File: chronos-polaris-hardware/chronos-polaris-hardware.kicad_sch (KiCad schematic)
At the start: 58 parts, among them J1 Conn_01x03_Pin, J2 Conn_01x03_Pin, J3 Conn_01x03_Pin, J4 Conn_01x03_Pin, J5 Conn_01x03_Pin, J6 Conn_01x04, J7 Conn_01x04, J8 Conn_01x02, P1 WJ124-3_81-6P, U1 TPS62172DSGR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

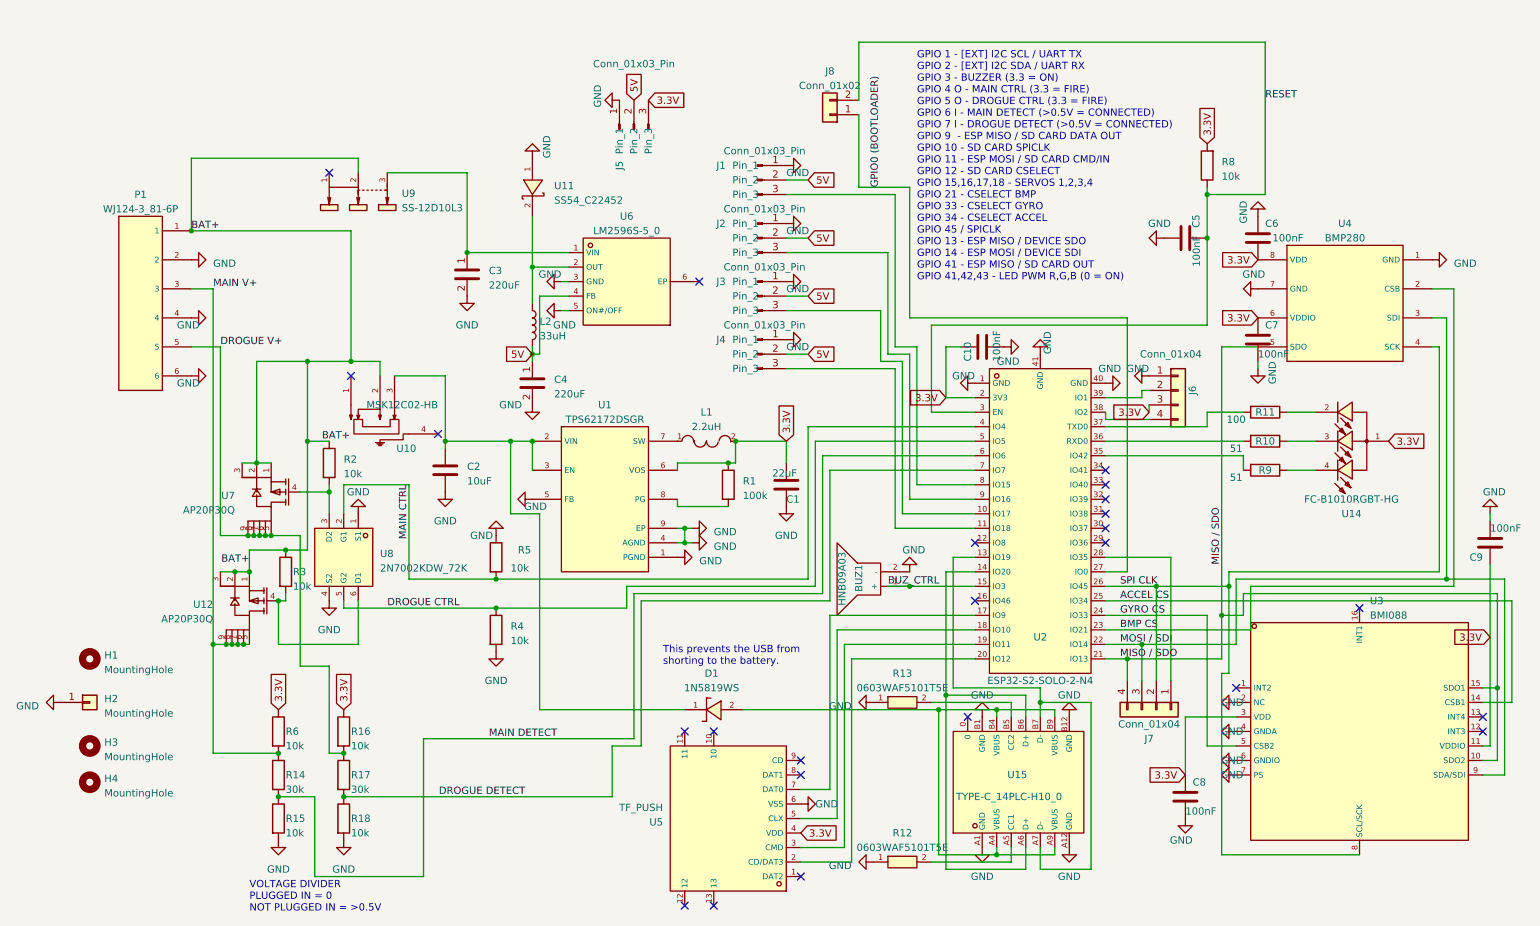
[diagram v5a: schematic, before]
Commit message: switch to compact 5v regulator
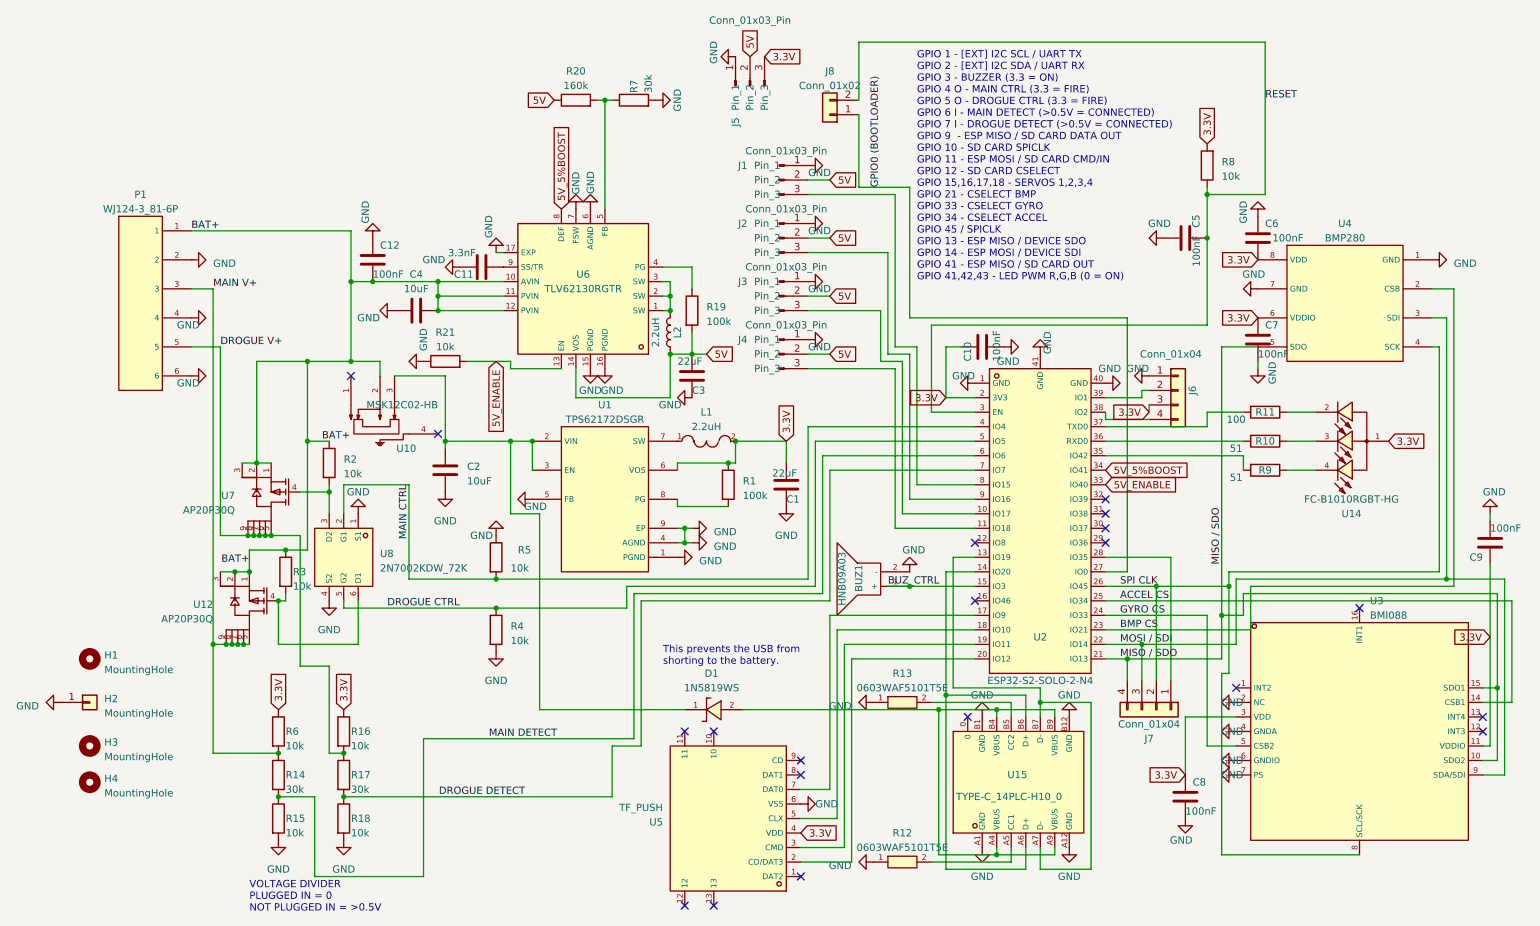
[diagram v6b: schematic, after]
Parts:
- removed U11: SS54_C22452, polaris-fp:SMA_L4.4-W2.8-LS5.4-R-RD, symbol polaris-sym:SS54_C22452
- removed U6: LM2596S-5_0, polaris-fp:TO-263-5_L10.2-W8.9-P1.70-BR, symbol polaris-sym:LM2596S-5_0
- removed U9: SS-12D10L3, polaris-fp:SW-TH_SS-12D10L3, symbol polaris-sym:SS-12D10L3
- added C11: 3.3nF, Capacitor_SMD:C_0402_1005Metric, symbol Device:C
- added C12: 100nF, Capacitor_SMD:C_0402_1005Metric, symbol Device:C
- added R19: 100k, Resistor_SMD:R_0603_1608Metric, symbol Device:R
- added R20: 160k, Resistor_SMD:R_0603_1608Metric, symbol Device:R
- added R21: 10k, Resistor_SMD:R_0603_1608Metric, symbol Device:R
- added R7: 30k, Resistor_SMD:R_0603_1608Metric, symbol Device:R
- added U6: TLV62130RGTR, polaris-fp:QFN-16_L3.0-W3.0-P0.50-TL-EP, symbol polaris-sym:TLV62130RGTR
- C3: value 220uF -> 22uF; footprint Capacitor_SMD:CP_Elec_8x10.5 -> Capacitor_SMD:C_0603_1608Metric
- C4: value 220uF -> 10uF; footprint Capacitor_SMD:CP_Elec_8x10.5 -> Capacitor_SMD:C_0805_2012Metric
- L2: value 33uH -> 2.2uH; footprint polaris-fp:IND-SMD_L11.5-W10.0_SMMS1040 -> polaris-fp:IND-SMD_L4.0-W4.0
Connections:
- net 5V: now also C3.1, L2.1, R19.2, R20.1, U6.14 (VOS); no longer C4.1, L2.2
- net BAT+: now also C4.1, C12.2, U6.10 (AVIN), U6.11 (PVIN), U6.12 (PVIN)
- net GND: now also C11.1, C12.1, R21.1, R7.2, U6.15 (PGND), U6.16 (PGND), U6.17 (EXP), U6.6 (AGND), U6.7 (FSW)
- net 5V_ENABLE: now reaches U2.33 (IO40)
- net 5V_ENABLE: now also R21.2, U6.13 (EN)
- net 5V_5%BOOST: now reaches U2.34 (IO41)
- net 5V_5%BOOST: now also U6.8 (DEF)
- new net: L2.2, U6.1 (SW), U6.2 (SW), U6.3 (SW)
- new net: R19.1, U6.4 (PG)
- new net: R20.2, R7.1, U6.5 (FB)
- new net: C11.2, U6.9 (SS/TR)
- no-connect marks 24 -> 20
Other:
- moved on the sheet: J1, J2, J3, J4, J5

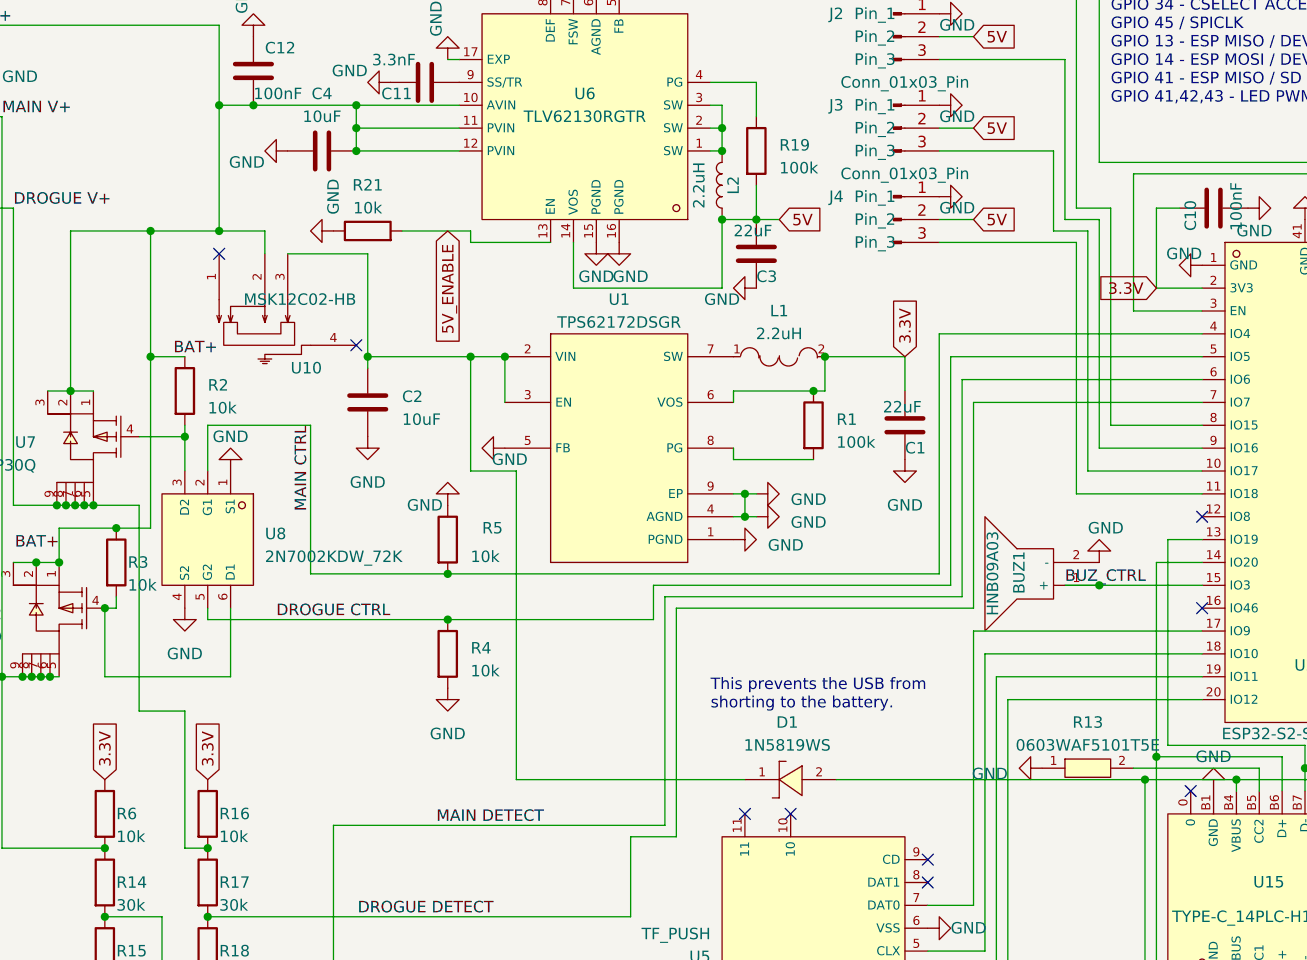
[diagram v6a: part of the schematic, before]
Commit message: fix V in switching with usb, remove diode
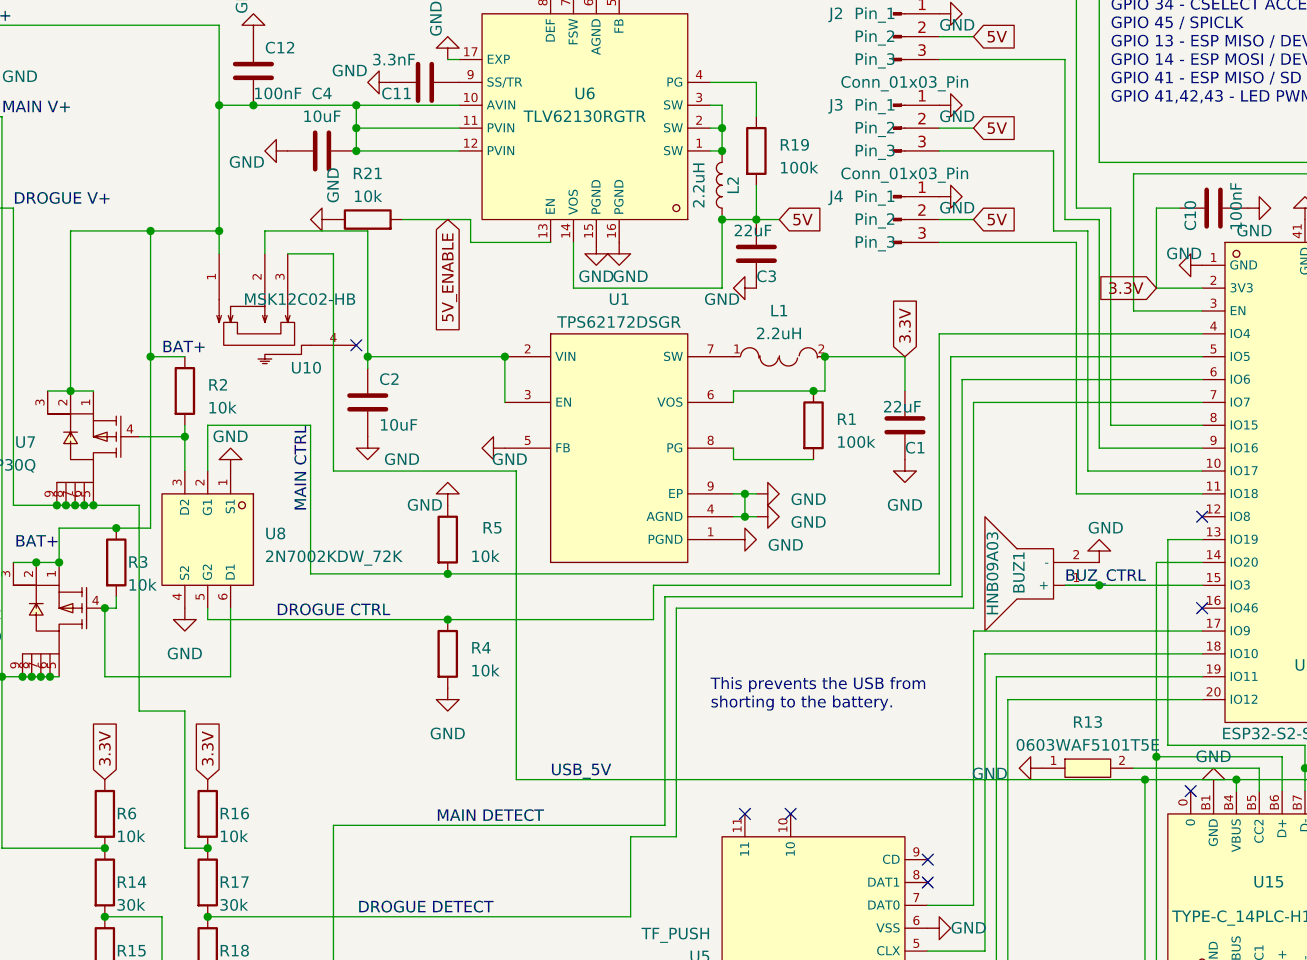
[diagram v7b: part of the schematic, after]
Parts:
- removed D1: 1N5819WS, polaris-fp:SOD-323_L1.8-W1.3-LS2.5-RD, symbol polaris-sym:1N5819WS
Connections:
- net BAT+: now also U10.1; no longer U10.2
- net at C2.1, U1.2 (VIN), U1.3 (EN): now also U10.2; no longer U10.3
- net USB_5V: now reaches U15.A4 (VBUS), U15.A9 (VBUS), U15.B4 (VBUS), U15.B9 (VBUS)
- net USB_5V: now also U10.3
- no-connect marks 20 -> 19
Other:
- moved on the sheet: R21
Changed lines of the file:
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@@
   (junction (at 194.31 137.16) (diameter 0) (color 0 0 0 0)
   )
-  (junction (at 109.22 90.17) (diameter 0) (color 0 0 0 0)
-  )
   (junction (at 80.01 144.78) (diameter 0) (color 0 0 0 0)
   )
@@
   (no_connect (at 160.02 148.59))
   (no_connect (at 257.81 119.38))
-  (no_connect (at 81.28 78.74))
   (wire (pts (xy 179.07 115.57) (xy 190.5 115.57))
     (stroke (width 0) (type default))
@@
     (stroke (width 0) (type default))
   )
-  (wire (pts (xy 86.36 76.2) (xy 86.36 78.74))
-    (stroke (width 0) (type default))
-  )
   (wire (pts (xy 166.37 156.21) (xy 166.37 123.19))
     (stroke (width 0) (type default))
@@
     (stroke (width 0) (type default))
   )
+  (wire (pts (xy 86.36 78.74) (xy 86.36 76.2))
+    (stroke (width 0) (type default))
+  )
   (wire (pts (xy 224.79 110.49) (xy 213.36 110.49))
     (stroke (width 0) (type default))
@@
     (stroke (width 0) (type default))
   )
-  (wire (pts (xy 73.66 90.17) (xy 77.47 90.17))
-    (stroke (width 0) (type default))
-  )
   (wire (pts (xy 139.7 105.41) (xy 139.7 107.95))
     (stroke (width 0) (type default))
@@
     (stroke (width 0) (type default))
   )
-  (wire (pts (xy 109.22 76.2) (xy 109.22 77.47))
+  (wire (pts (xy 109.22 74.93) (xy 109.22 77.47))
     (stroke (width 0) (type default))
   )
@@
     (stroke (width 0) (type default))
   )
+  (wire (pts (xy 73.66 90.17) (xy 77.47 90.17))
+    (stroke (width 0) (type default))
+  )
   (wire (pts (xy 233.68 73.66) (xy 233.68 120.65))
     (stroke (width 0) (type default))
@@
     (stroke (width 0) (type default))
   )
-  (wire (pts (xy 109.22 102.87) (xy 109.22 90.17))
-    (stroke (width 0) (type default))
-  )
   (wire (pts (xy 62.23 93.98) (xy 64.77 93.98))
     (stroke (width 0) (type default))
@@
     (stroke (width 0) (type default))
   )
-  (wire (pts (xy 109.22 90.17) (xy 113.03 90.17))
+  (wire (pts (xy 97.79 90.17) (xy 113.03 90.17))
     (stroke (width 0) (type default))
   )
@@
     (stroke (width 0) (type default))
   )
-  (wire (pts (xy 114.3 102.87) (xy 109.22 102.87))
-    (stroke (width 0) (type default))
-  )
   (wire (pts (xy 74.93 152.4) (xy 68.58 152.4))
     (stroke (width 0) (type default))
@@
     (stroke (width 0) (type default))
   )
+  (wire (pts (xy 93.98 78.74) (xy 88.9 78.74))
+    (stroke (width 0) (type default))
+  )
   (wire (pts (xy 60.96 113.03) (xy 63.5 113.03))
     (stroke (width 0) (type default))
@@
     (stroke (width 0) (type default))
   )
+  (wire (pts (xy 93.98 102.87) (xy 114.3 102.87))
+    (stroke (width 0) (type default))
+  )
+  (wire (pts (xy 81.28 76.2) (xy 81.28 78.74))
+    (stroke (width 0) (type default))
+  )
   (wire (pts (xy 130.81 116.84) (xy 163.83 116.84))
     (stroke (width 0) (type default))
@@
     (stroke (width 0) (type default))
   )
-  (wire (pts (xy 82.55 125.73) (xy 82.55 118.11))
+  (wire (pts (xy 86.36 76.2) (xy 97.79 76.2))
     (stroke (width 0) (type default))
   )
-  (wire (pts (xy 88.9 78.74) (xy 97.79 78.74))
+  (wire (pts (xy 82.55 125.73) (xy 82.55 118.11))
     (stroke (width 0) (type default))
   )
@@
     (stroke (width 0) (type default))
   )
+  (wire (pts (xy 93.98 102.87) (xy 93.98 78.74))
+    (stroke (width 0) (type default))
+  )
   (wire (pts (xy 160.02 163.83) (xy 168.91 163.83))
     (stroke (width 0) (type default))
@@
     (stroke (width 0) (type default))
   )
-  (wire (pts (xy 97.79 90.17) (xy 109.22 90.17))
-    (stroke (width 0) (type default))
-  )
   (wire (pts (xy 238.76 123.19) (xy 238.76 115.57))
     (stroke (width 0) (type default))
@@
     (stroke (width 0) (type default))
   )
-  (wire (pts (xy 139.7 137.16) (xy 114.3 137.16))
+  (wire (pts (xy 114.3 137.16) (xy 184.15 137.16))
     (stroke (width 0) (type default))
   )
@@
     (stroke (width 0) (type default))
   )
-  (wire (pts (xy 86.36 76.2) (xy 81.28 76.2))
-    (stroke (width 0) (type default))
-  )
   (wire (pts (xy 163.83 92.71) (xy 190.5 92.71))
     (stroke (width 0) (type default))
@@
     (stroke (width 0) (type default))
   )
-  (wire (pts (xy 97.79 78.74) (xy 97.79 90.17))
-    (stroke (width 0) (type default))
-  )
   (wire (pts (xy 165.1 54.61) (xy 161.29 54.61))
     (stroke (width 0) (type default))
@@
     (stroke (width 0) (type default))
   )
-  (wire (pts (xy 101.6 76.2) (xy 109.22 76.2))
-    (stroke (width 0) (type default))
-  )
-  (wire (pts (xy 149.86 137.16) (xy 184.15 137.16))
+  (wire (pts (xy 101.6 74.93) (xy 109.22 74.93))
     (stroke (width 0) (type default))
   )
@@
     (stroke (width 0) (type default))
   )
+  (wire (pts (xy 97.79 76.2) (xy 97.79 90.17))
+    (stroke (width 0) (type default))
+  )
   (wire (pts (xy 148.59 90.17) (xy 148.59 93.98))
     (stroke (width 0) (type default))
@@
     (effects (font (size 1.27 1.27)) (justify right bottom))
   )
+  (label "USB_5V" (at 118.11 137.16 0) (fields_autoplaced)
+    (effects (font (size 1.27 1.27)) (justify left bottom))
+  )
   (label "MAIN CTRL" (at 91.44 97.79 270) (fields_autoplaced)
     (effects (font (size 1.27 1.27)) (justify right bottom))
@@
     (effects (font (size 1.27 1.27)) (justify left bottom))
   )
-  (label "BAT+" (at 76.2 90.17 0) (fields_autoplaced)
+  (label "BAT+" (at 74.93 90.17 0) (fields_autoplaced)
     (effects (font (size 1.27 1.27)) (justify left bottom))
   )
@@
     (effects (font (size 1.27 1.27)) (justify left bottom))
   )
-  (global_label "5V_ENABLE" (shape input) (at 106.68 76.2 270) (fields_autoplaced)
+  (global_label "5V_ENABLE" (shape input) (at 106.68 74.93 270) (fields_autoplaced)
     (effects (font (size 1.27 1.27)) (justify right))
-    (property "Intersheetrefs" "${INTERSHEET_REFS}" (at 106.68 89.3867 90)
+    (property "Intersheetrefs" "${INTERSHEET_REFS}" (at 106.68 88.1167 90)
       (effects (font (size 1.27 1.27)) (justify right) hide)
     )
@@
     )
   )
-  (symbol (lib_id "polaris-sym:1N5819WS") (at 144.78 137.16 0) (unit 1)
-    (in_bom yes) (on_board yes) (dnp no) (fields_autoplaced)
-    (property "Reference" "D1" (at 144.399 130.81 0)
-      (effects (font (size 1.27 1.27)))
-    )
-    (property "Value" "1N5819WS" (at 144.399 133.35 0)
-      (effects (font (size 1.27 1.27)))
-    )
-    (property "Footprint" "polaris-fp:SOD-323_L1.8-W1.3-LS2.5-RD" (at 144.78 147.32 0)
-      (effects (font (size 1.27 1.27) italic) hide)
-    )
-    (property "Datasheet" "https://item.szlcsc.com/295156.html" (at 142.494 137.033 0)
-      (effects (font (size 1.27 1.27)) (justify left) hide)
-    )
-    (property "LCSC" "C191023" (at 144.78 137.16 0)
-      (effects (font (size 1.27 1.27)) hide)
-    )
-    (pin "1")
-    (pin "2")
-    (instances
-      (project "chronos-polaris-hardware"
-        (path "/503f01d5-a0c6-4ade-b485-97c3c2e1d6c5"
-          (reference "D1") (unit 1)
-        )
-      )
-    )
-  )
   (symbol (lib_id "power:GND") (at 97.79 99.06 0) (unit 1)
-    (in_bom yes) (on_board yes) (dnp no) (fields_autoplaced)
+    (in_bom yes) (on_board yes) (dnp no)
     (property "Reference" "#PWR016" (at 97.79 105.41 0)
       (effects (font (size 1.27 1.27)) hide)
     )
-    (property "Value" "GND" (at 97.79 104.14 0)
+    (property "Value" "GND" (at 101.6 101.6 0)
       (effects (font (size 1.27 1.27)))
     )
@@
   )
   (symbol (lib_id "Device:C") (at 97.79 95.25 0) (unit 1)
-    (in_bom yes) (on_board yes) (dnp no) (fields_autoplaced)
-    (property "Reference" "C2" (at 101.6 94.615 0)
+    (in_bom yes) (on_board yes) (dnp no)
+    (property "Reference" "C2" (at 99.06 92.71 0)
       (effects (font (size 1.27 1.27)) (justify left))
     )
-    (property "Value" "10uF" (at 101.6 97.155 0)
+    (property "Value" "10uF" (at 99.06 97.79 0)
       (effects (font (size 1.27 1.27)) (justify left))
     )
@@
     )
   )
-  (symbol (lib_id "Device:R") (at 97.79 76.2 90) (unit 1)
+  (symbol (lib_id "Device:R") (at 97.79 74.93 90) (unit 1)
     (in_bom yes) (on_board yes) (dnp no) (fields_autoplaced)
-    (property "Reference" "R21" (at 97.79 71.12 90)
+    (property "Reference" "R21" (at 97.79 69.85 90)
       (effects (font (size 1.27 1.27)))
     )
-    (property "Value" "10k" (at 97.79 73.66 90)
+    (property "Value" "10k" (at 97.79 72.39 90)
       (effects (font (size 1.27 1.27)))
     )
-    (property "Footprint" "Resistor_SMD:R_0603_1608Metric" (at 97.79 77.978 90)
+    (property "Footprint" "Resistor_SMD:R_0603_1608Metric" (at 97.79 76.708 90)
       (effects (font (size 1.27 1.27)) hide)
     )
-    (property "Datasheet" "~" (at 97.79 76.2 0)
+    (property "Datasheet" "~" (at 97.79 74.93 0)
       (effects (font (size 1.27 1.27)) hide)
     )
@@
     )
   )
-  (symbol (lib_id "power:GND") (at 93.98 76.2 270) (unit 1)
+  (symbol (lib_id "power:GND") (at 93.98 74.93 270) (unit 1)
     (in_bom yes) (on_board yes) (dnp no)
-    (property "Reference" "#PWR019" (at 87.63 76.2 0)
+    (property "Reference" "#PWR019" (at 87.63 74.93 0)
       (effects (font (size 1.27 1.27)) hide)
     )
-    (property "Value" "GND" (at 93.98 72.39 0)
+    (property "Value" "GND" (at 93.98 71.12 0)
       (effects (font (size 1.27 1.27)))
     )
-    (property "Footprint" "" (at 93.98 76.2 0)
+    (property "Footprint" "" (at 93.98 74.93 0)
       (effects (font (size 1.27 1.27)) hide)
     )
-    (property "Datasheet" "" (at 93.98 76.2 0)
+    (property "Datasheet" "" (at 93.98 74.93 0)
       (effects (font (size 1.27 1.27)) hide)
     )
